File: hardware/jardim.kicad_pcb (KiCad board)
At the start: 2 copper layers, 100 x 100 mm, 81 parts, among them J1 DC_INPUT, J10 DHT22_AMB, J11 LIGHT_SENSOR_1, J12 LIGHT_SENSOR_2, J13 LEVEL_SENSOR_1, J14 LEVEL_SENSOR_2, J15 SOIL_HUMIDITY_SENSOR_1, J16 SOIL_HUMIDITY_SENSOR_2, J2 PUMP_1, J3 PUMP_2, J4 LIGHT_1, J5 LIGHT_2, J6 HEAT_1, J7 HEAT_2, J8 DS12B20_2, J9 DS18B20_1, Q1 FQP30N06L, Q2 FQP30N06L, Q3 FQP30N06L, Q4 FQP30N06L, Q5 FQP30N06L, Q6 FQP30N06L, Q7 BC337, SW1 SW_Push, SW2 SW_Push, SW3 SW_Push, SW4 SW_SPST, U1 AM2302, U2 DM-OLED096-636

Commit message: corrigido todos os modulos perifericos
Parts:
- removed C3, C6: 100uF 25V, Capacitor_THT:CP_Radial_D6.3mm_P2.50mm
- removed C4, C5: 100nF 50V, Capacitor_THT:C_Disc_D5.0mm_W2.5mm_P5.00mm
- H1: renamed from h1; value MountingHole_3.2mm_M3_Pad_Via -> MountingHole_Pad
- H2: renamed from h2; value MountingHole_3.2mm_M3_Pad_Via -> MountingHole_Pad
- H3: renamed from h3; value MountingHole_3.2mm_M3_Pad_Via -> MountingHole_Pad
- H4: renamed from h4; value MountingHole_3.2mm_M3_Pad_Via -> MountingHole_Pad
- J5: value LIGHT_2 -> LIGHG_2
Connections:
- net Net-(D1-A) renamed /PUMP_1_SW_NEG
- net Net-(D3-A) renamed /PUMP_2_SW_NEG
- net Net-(D6-K) renamed /LIGHT_1_SW_NEG
- net Net-(D7-K) renamed /LIGHT_2_SW_NEG
- net Net-(D8-K) renamed /HEATER_1_SW_NEG
- net Net-(D9-K) renamed /HEATER_2_SW_NEG
- H1 pad 1: (no net) -> GND
- H2 pad 1: (no net) -> GND
- H3 pad 1: (no net) -> GND
- H4 pad 1: (no net) -> GND
- R3 pad 1: +12V -> Net-(D2-A)
- R3 pad 2: Net-(D2-A) -> +12V
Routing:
- net +12V: track 286.4 -> 0.00 mm, vias 1 -> 0
- net +5V: track 241.2 -> 0.00 mm, vias 1 -> 0
- net +24V: track 194.4 -> 0.00 mm, vias 1 -> 0
- net /IO37: track 124.4 -> 0.00 mm
- net /IO11: track 98.3 -> 0.00 mm
- net /PUMP_2_SW_NEG: track 93.0 -> 0.00 mm
- net /IO9: track 76.6 -> 0.00 mm, vias 1 -> 0
- net /IO18: track 73.2 -> 0.00 mm
- net /IO12: track 66.2 -> 0.00 mm, vias 1 -> 0
- net /IO8: track 64.7 -> 0.00 mm, vias 1 -> 0
- net /IO36: track 59.2 -> 0.00 mm, vias 1 -> 0
- net /IO35: track 58.7 -> 0.00 mm
- net /IO10: track 58.6 -> 0.00 mm
- net /IO1: track 58.1 -> 0.00 mm, vias 1 -> 0
- net /IO17: track 55.8 -> 0.00 mm
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- removed copper zone on B.Cu, net GND
- removed copper zone on F.Cu, net GND

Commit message: lemure e usb c
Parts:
- added J18: USB_C_Receptacle_PowerOnly_6P, Connector_USB:USB_C_Receptacle_GCT_USB4125-xx-x_6P_TopMnt_Horizontal, F.Cu at (188.6, 118.7)
- added R22: 5.1k, Resistor_THT:R_Axial_DIN0207_L6.3mm_D2.5mm_P10.16mm_Horizontal, B.Cu at (163.0, 90.4)
- added R23: 5.1k, Resistor_THT:R_Axial_DIN0207_L6.3mm_D2.5mm_P10.16mm_Horizontal, B.Cu at (163.0, 94.5)
- moved H4 13.7 mm to (187.7, 132.1)
- moved SW1 8.25 mm to (175.2, 114.6)
- moved SW2 8.25 mm to (175.2, 122.2)
- moved SW3 8.25 mm to (175.2, 129.8)
- moved C2 2.59 mm to (170.8, 65.4)
- moved C1 1.27 mm to (164.5, 66.6)
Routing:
- net GND: track 0.00 -> 594.7 mm, vias 0 -> 1
- net +5V: track 0.00 -> 240.6 mm
- net +12V: track 0.00 -> 235.8 mm, vias 0 -> 2
- net +24V: track 0.00 -> 199.8 mm, vias 0 -> 1
- net /IO11: track 0.00 -> 107.0 mm
- net /PUMP_2_SW_NEG: track 0.00 -> 101.6 mm, vias 0 -> 1
- net /IO9: track 0.00 -> 89.7 mm, vias 0 -> 1
- net /IO18: track 0.00 -> 77.3 mm
- net /IO8: track 0.00 -> 70.0 mm, vias 0 -> 1
- net Net-(J18-CC1): track 0.00 -> 69.6 mm
- net /IO36: track 0.00 -> 63.0 mm, vias 0 -> 1
- net /IO35: track 0.00 -> 60.8 mm
- net /IO10: track 0.00 -> 58.4 mm
- net /IO13: track 0.00 -> 57.3 mm
- net /IO17: track 0.00 -> 56.1 mm
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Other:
- board text added: "Projetado no Brasil"
- board text removed: "DOWN"
- board text removed: "UP"

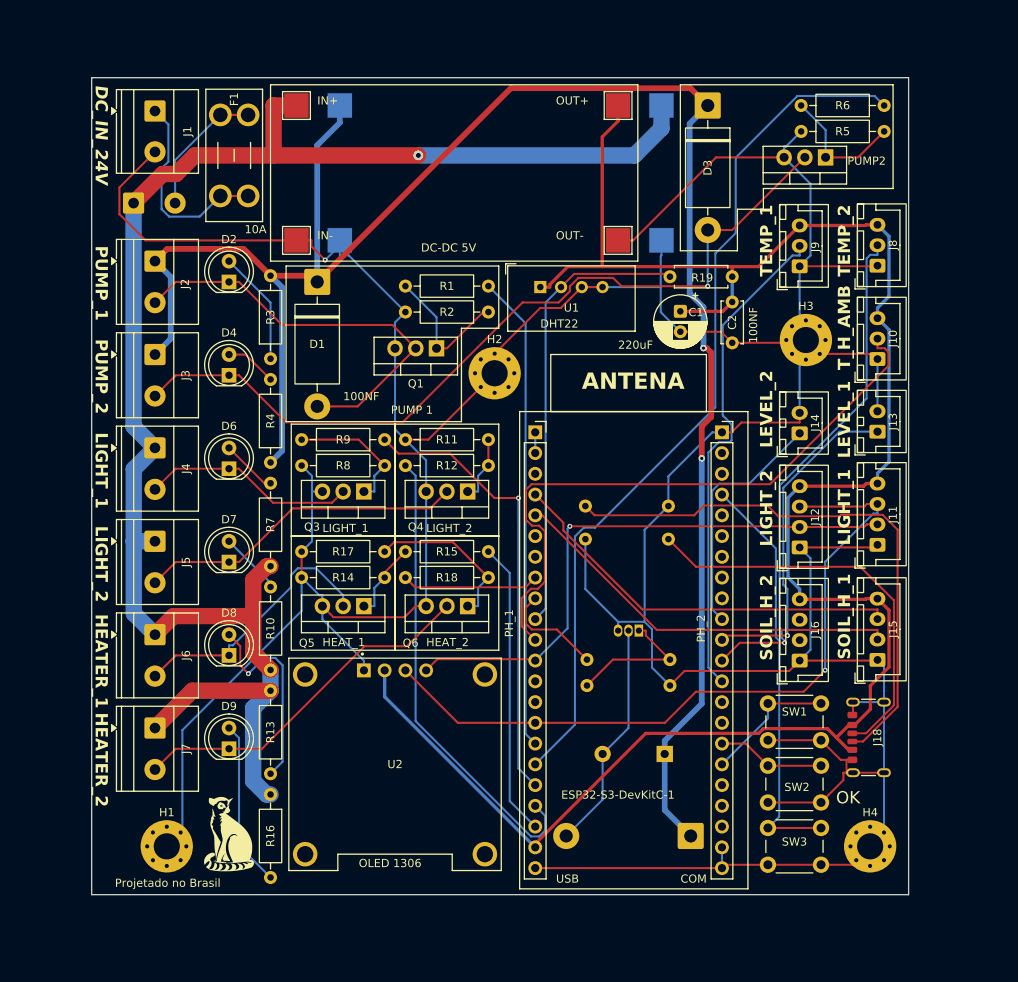
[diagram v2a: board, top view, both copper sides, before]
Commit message: pull up sensores, debaunce botoes
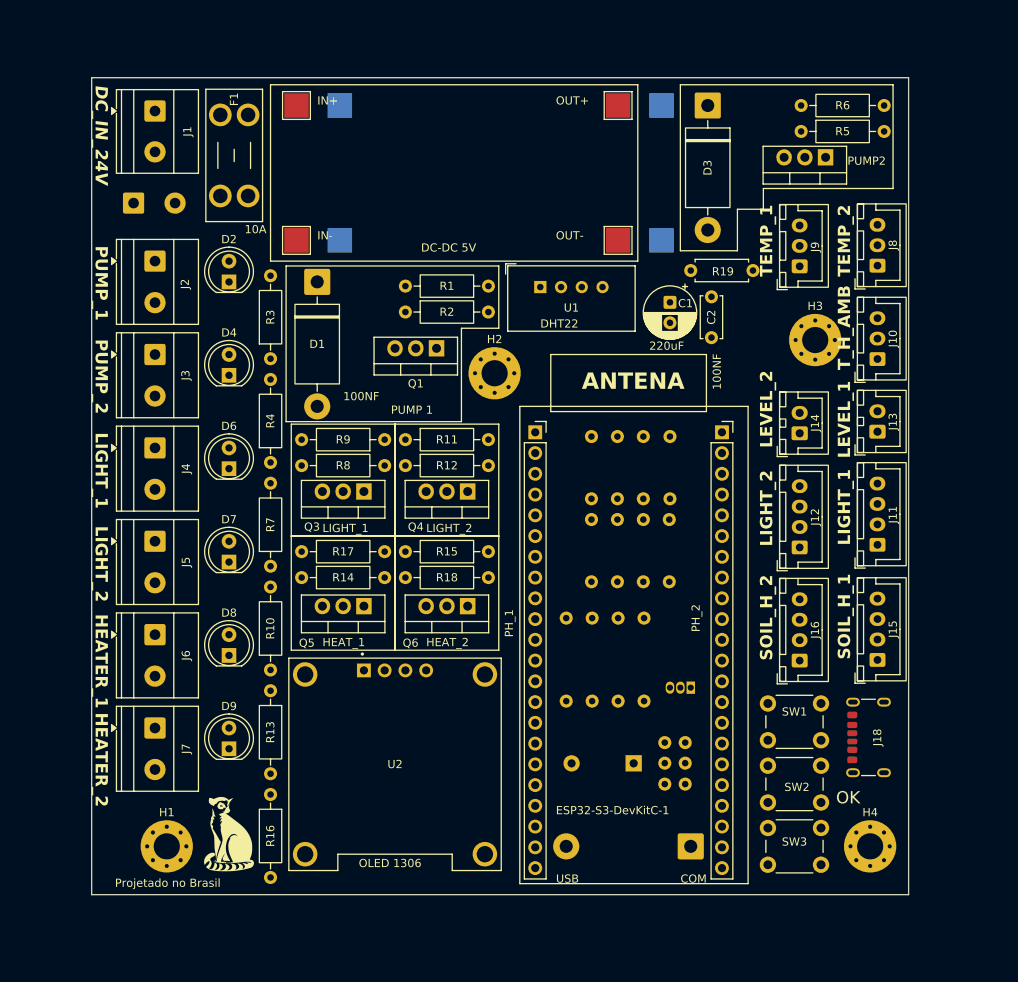
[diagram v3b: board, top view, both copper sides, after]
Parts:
- added C3: 100nf, Capacitor_THT:C_Disc_D3.0mm_W1.6mm_P2.50mm, B.Cu at (165.1, 119.4)
- added C4: 100nf, Capacitor_THT:C_Disc_D3.0mm_W1.6mm_P2.50mm, B.Cu at (165.1, 121.9)
- added C5: 100nf, Capacitor_THT:C_Disc_D3.0mm_W1.6mm_P2.50mm, B.Cu at (165.1, 124.5)
- added R27: 4.7k, Resistor_THT:R_Axial_DIN0207_L6.3mm_D2.5mm_P7.62mm_Horizontal, B.Cu at (163.2, 89.5)
- added R28: 4.7k, Resistor_THT:R_Axial_DIN0207_L6.3mm_D2.5mm_P7.62mm_Horizontal, B.Cu at (159.9, 89.5)
- added R29: 4.7k, Resistor_THT:R_Axial_DIN0207_L6.3mm_D2.5mm_P7.62mm_Horizontal, B.Cu at (156.8, 89.5)
- added R30: 4.7k, Resistor_THT:R_Axial_DIN0207_L6.3mm_D2.5mm_P7.62mm_Horizontal, B.Cu at (153.6, 89.5)
- added R31: 1k, Resistor_THT:R_Axial_DIN0207_L6.3mm_D2.5mm_P7.62mm_Horizontal, B.Cu at (153.6, 92.1)
- added R32: 1k, Resistor_THT:R_Axial_DIN0207_L6.3mm_D2.5mm_P7.62mm_Horizontal, B.Cu at (156.8, 92.1)
- added R33: 1k, Resistor_THT:R_Axial_DIN0207_L6.3mm_D2.5mm_P7.62mm_Horizontal, B.Cu at (159.9, 92.1)
- added R34: 1k, Resistor_THT:R_Axial_DIN0207_L6.3mm_D2.5mm_P7.62mm_Horizontal, B.Cu at (163.1, 92.1)
- F1: value 15A -> 10A
- moved R23 20.0 mm to (160.0, 114.3), turned to 90 degrees
- moved R22 15.0 mm to (156.8, 104.1), turned to -90 degrees
- moved R20 13.7 mm to (150.5, 104.1), turned to -90 degrees
- moved R21 12.6 mm to (153.7, 104.1), turned to -90 degrees
- moved Q7 9.44 mm to (165.7, 112.7)
- moved BZ1 3.97 mm to (158.8, 121.9)
- moved R19 2.65 mm to (173.4, 61.6)
- moved C2 2.62 mm to (168.3, 64.8)
- moved C1 1.68 mm to (163.2, 65.5)
- moved D5 1.27 mm to (165.7, 132.1)
- moved H3 1.14 mm to (181.0, 70.1)
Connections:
- net Net-(J1-Pin_1) renamed /VIN_RAW
- J15 pad 2: /IO5 -> unconnected-(J15-Pin_2-Pad2)
- J15 pad 3: /IO4 -> /IO5
- J16 pad 3: unconnected-(J16-Pin_3-Pad3) -> /IO4
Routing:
- net GND: track 594.7 -> 0.00 mm, vias 1 -> 0
- net +5V: track 240.6 -> 0.00 mm
- net +12V: track 235.8 -> 0.00 mm, vias 2 -> 0
- net +24V: track 199.8 -> 0.00 mm, vias 1 -> 0
- net /IO11: track 107.0 -> 0.00 mm
- net /PUMP_2_SW_NEG: track 101.6 -> 0.00 mm, vias 1 -> 0
- net /IO9: track 89.7 -> 0.00 mm, vias 1 -> 0
- net /IO18: track 77.3 -> 0.00 mm
- net /IO8: track 70.0 -> 0.00 mm, vias 1 -> 0
- net Net-(J18-CC1): track 69.6 -> 0.00 mm
- net /IO36: track 63.0 -> 0.00 mm, vias 1 -> 0
- net /IO35: track 60.8 -> 0.00 mm
- net /IO10: track 58.4 -> 0.00 mm
- net /IO13: track 57.3 -> 0.00 mm
- net /IO17: track 56.1 -> 0.00 mm
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
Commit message: ajustes
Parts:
- removed R2: 10k, Resistor_THT:R_Axial_DIN0207_L6.3mm_D2.5mm_P10.16mm_Horizontal
- moved U2 1.35 mm to (129.5, 123.4)
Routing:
- added copper zone on B.Cu, net GND
- added copper zone on F.Cu, net GND
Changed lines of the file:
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@@
 	(footprint "oled:MODULE_DM-OLED096-636"
 		(layer "F.Cu")
-		(at 129.54 122.04)
+		(at 129.54 123.395)
 		(property "Reference" "U2"
 			(at 0 0 0)
@@
 	(footprint "Capacitor_THT:CP_Radial_D6.3mm_P2.50mm"
 		(layer "F.Cu")
-		(at 163.195 65.492621 -90)
+		(at 163.195 65.4926 -90)
 		(descr "CP, Radial series, Radial, pin pitch=2.50mm, diameter=6.3mm, height=7mm, Electrolytic Capacitor")
 		(tags "CP Radial series Radial pin pitch 2.50mm diameter 6.3mm height 7mm Electrolytic Capacitor")
@@
 		)
 	)
-	(footprint "Resistor_THT:R_Axial_DIN0207_L6.3mm_D2.5mm_P10.16mm_Horizontal"
-		(layer "F.Cu")
-		(at 130.81 66.675)
-		(descr "Resistor, Axial_DIN0207 series, Axial, Horizontal, pin pitch=10.16mm, 0.25W = 1/4W, length*diameter=6.3*2.5mm^2, http://cdn-reichelt.de/documents/datenblatt/B400/1_4W%23YAG.pdf")
-		(tags "Resistor Axial_DIN0207 series Axial Horizontal pin pitch 10.16mm 0.25W = 1/4W length 6.3mm diameter 2.5mm")
-		(property "Reference" "R2"
-			(at 5.08 0 0)
-			(layer "F.SilkS")
-			(effects
-				(font
-					(size 1 1)
-					(thickness 0.15)
-				)
-			)
-		)
-		(property "Value" "10k"
-			(at 5.08 2.37 0)
-			(layer "F.Fab")
-			(effects
-				(font
-					(size 1 1)
-					(thickness 0.15)
-				)
-			)
-		)
-		(property "Datasheet" ""
-			(at 0 0 0)
-			(layer "F.Fab")
-			(hide yes)
-			(effects
-				(font
-					(size 1.27 1.27)
-				)
-			)
-		)
-		(property "Description" "Resistor"
-			(at 0 0 0)
-			(layer "F.Fab")
-			(hide yes)
-			(effects
-				(font
-					(size 1.27 1.27)
-				)
-			)
-		)
-		(property ki_fp_filters "R_*")
-		(sheetname "/")
-		(sheetfile "jardim.kicad_sch")
-		(units
-			(unit
-				(name "A")
-				(pins "1" "2")
-			)
-		)
-		(attr through_hole)
-		(duplicate_pad_numbers_are_jumpers no)
-		(fp_line
-			(start 1.04 0)
-			(end 1.81 0)
-			(stroke
-				(width 0.12)
-				(type solid)
-			)
-			(layer "F.SilkS")
-		)
-		(fp_line
-			(start 9.12 0)
-			(end 8.35 0)
-			(stroke
-				(width 0.12)
-				(type solid)
-			)
-			(layer "F.SilkS")
-		)
-		(fp_rect
-			(start 1.81 -1.37)
-			(end 8.35 1.37)
-			(stroke
-				(width 0.12)
-				(type solid)
-			)
-			(fill no)
-			(layer "F.SilkS")
-		)
-		(fp_rect
-			(start -1.05 -1.5)
-			(end 11.21 1.5)
-			(stroke
-				(width 0.05)
-				(type solid)
-			)
-			(fill no)
-			(layer "F.CrtYd")
-		)
-		(fp_line
-			(start 0 0)
-			(end 1.93 0)
-			(stroke
-				(width 0.1)
-				(type solid)
-			)
-			(layer "F.Fab")
-		)
-		(fp_line
-			(start 10.16 0)
-			(end 8.23 0)
-			(stroke
-				(width 0.1)
-				(type solid)
-			)
-			(layer "F.Fab")
-		)
-		(fp_rect
-			(start 1.93 -1.25)
-			(end 8.23 1.25)
-			(stroke
-				(width 0.1)
-				(type solid)
-			)
-			(fill no)
-			(layer "F.Fab")
-		)
-		(fp_text user "${REFERENCE}"
-			(at 5.08 0 0)
-			(layer "F.Fab")
-			(effects
-				(font
-					(size 1 1)
-					(thickness 0.15)
-				)
-			)
-		)
-		(pad "1" thru_hole circle
-			(at 0 0)
-			(size 1.6 1.6)
-			(drill 0.8)
-			(layers "*.Cu" "*.Mask")
-			(remove_unused_layers no)
-			(net "GND")
-			(pintype "passive")
-		)
-		(pad "2" thru_hole circle
-			(at 10.16 0)
-			(size 1.6 1.6)
-			(drill 0.8)
-			(layers "*.Cu" "*.Mask")
-			(remove_unused_layers no)
-			(net "Net-(Q1-G)")
-			(pintype "passive")
-		)
-		(embedded_fonts no)
-		(model "kicad-embed://R_Axial_DIN0207_L6.3mm_D2.5mm_P10.16mm_Horizontal.step"
-			(offset
-				(xyz 0 0 0)
-			)
-			(scale
-				(xyz 1 1 1)
-			)
-			(rotate
-				(xyz 0 0 0)
-			)
-		)
-	)
 	(footprint "Button_Switch_THT:SW_PUSH_6mm"
 		(layer "F.Cu")
@@
 		(sheetname "/")
 		(sheetfile "jardim.kicad_sch")
+		(units
+			(unit
+				(name "A")
+				(pins "1" "2")
+			)
+		)
 		(attr through_hole)
 		(duplicate_pad_numbers_are_jumpers no)
@@
 		(sheetname "/")
 		(sheetfile "jardim.kicad_sch")
+		(units
+			(unit
+				(name "A")
+				(pins "1" "2")
+			)
+		)
 		(attr through_hole)
 		(duplicate_pad_numbers_are_jumpers no)
@@
 		(sheetname "/")
 		(sheetfile "jardim.kicad_sch")
+		(units
+			(unit
+				(name "A")
+				(pins "1" "2")
+			)
+		)
 		(attr through_hole)
 		(duplicate_pad_numbers_are_jumpers no)
@@
 	)
 	(gr_text "OLED 1306"
-		(at 125.095 134.74 0)
+		(at 125.095 136.095 0)
 		(layer "F.SilkS")
 		(effects
@@
 			)
 		)
+	)
+	(zone
+		(net "GND")
+		(layers "F.Cu" "B.Cu")
+		(hatch edge 0.5)
+		(connect_pads
+			(clearance 0.5)
+		)
+		(min_thickness 0.25)
+		(fill yes
+			(thermal_gap 0.5)
+			(thermal_bridge_width 0.5)
+			(island_removal_mode 0)
+		)
+		(polygon
+			(pts
+				(xy 83.185 31.115) (xy 83.185 146.05) (xy 203.835 146.685) (xy 202.565 30.48)
+			)
+		)

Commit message: sem avisos, pronto para rotear
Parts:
- added R2: 10k, Resistor_THT:R_Axial_DIN0207_L6.3mm_D2.5mm_P10.16mm_Horizontal, F.Cu at (124.5, 67.3)
- moved R19 19.1 mm to (154.3, 62.9), turned to 0 degrees
- moved R5 6.71 mm to (172.5, 44.3)
- moved R6 6.71 mm to (182.7, 41.2)
- moved U1 6.37 mm to (141.0, 64.1)
- moved R1 6.35 mm to (134.6, 63.5)
- moved C2 4.93 mm to (172.1, 61.7)
- moved C1 4.61 mm to (167.0, 62.9)
- moved Q1 3.18 mm to (131.4, 71.1)
- moved Q2 2.72 mm to (179.5, 47.6)
- moved J2 1.91 mm to (98.3, 60.4)
- moved J3 1.91 mm to (98.3, 71.9)
- moved J4 1.91 mm to (98.3, 83.3)
- moved J5 1.91 mm to (98.3, 94.7)
- moved J6 1.91 mm to (98.3, 106.2)
- moved J7 1.91 mm to (98.3, 117.6)
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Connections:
- net Net-(SW4-B) renamed /VIN_AFTER_FUSE
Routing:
- net +24V: track 0.00 -> 257.2 mm
- net +12V: track 0.00 -> 244.2 mm, vias 0 -> 1
- net +5V: track 0.00 -> 243.7 mm
- net /IO11: track 0.00 -> 102.0 mm, vias 0 -> 1
- net /PUMP_2_SW_NEG: track 0.00 -> 94.7 mm
- net /IO9: track 0.00 -> 77.9 mm
- net /IO36: track 0.00 -> 72.7 mm, vias 0 -> 1
- net /IO10: track 0.00 -> 70.0 mm, vias 0 -> 1
- net /IO17: track 0.00 -> 68.5 mm, vias 0 -> 2
- net /IO37: track 0.00 -> 68.3 mm, vias 0 -> 1
- net /IO18: track 0.00 -> 67.9 mm
- net /IO1: track 0.00 -> 67.4 mm
- net /IO35: track 0.00 -> 65.0 mm
- net /IO8: track 0.00 -> 63.7 mm
- net /IO38: track 0.00 -> 54.3 mm
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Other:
- board text removed: "10k"

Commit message: netlist completa
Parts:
- moved H3 0.50 mm to (179.7, 70.5)
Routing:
- net +24V: track 257.2 -> 157.5 mm, vias 0 -> 1
- net +5V: track 243.7 -> 203.4 mm, vias 0 -> 1
- net /IO36: track 72.7 -> 32.9 mm
- net +12V: track 244.2 -> 263.2 mm, vias 1 -> 0
- net /IO18: track 67.9 -> 78.7 mm, vias 0 -> 1
- net Net-(D8-A): track 19.1 -> 29.9 mm
- net /IO12: track 53.8 -> 63.9 mm, vias 1 -> 0
- net /IO16: track 23.4 -> 14.2 mm
- net /IO10: track 70.0 -> 61.1 mm, vias 1 -> 0
- net /IO11: track 102.0 -> 110.6 mm, vias 1 -> 0
- net /IO38: track 54.3 -> 61.7 mm
- net /IO17: track 68.5 -> 61.4 mm, vias 2 -> 0
- net Net-(J18-CC1): track 31.7 -> 38.6 mm
- net /IO9: track 77.9 -> 84.2 mm, vias 0 -> 1
- net /IO35: track 65.0 -> 71.1 mm, vias 0 -> 1
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
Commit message: 0 erros. 100%
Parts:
- moved R6 10.2 mm to (172.5, 40.9), turned to 0 degrees
- moved C3 1.73 mm to (165.6, 117.1)
- moved H3 1.45 mm to (178.8, 69.3)
- moved C1 1.41 mm to (166.6, 64.3)
- moved C5 1.26 mm to (165.6, 125.0)
- moved C4 0.62 mm to (165.6, 120.9)
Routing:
- net +5V: track 203.4 -> 271.1 mm
- net +24V: track 157.5 -> 212.0 mm
- net /IO36: track 32.9 -> 85.1 mm, vias 1 -> 0
- net +12V: track 263.2 -> 240.5 mm
- net /IO11: track 110.6 -> 125.5 mm
- net /IO18: track 78.7 -> 64.0 mm
- net /IO12: track 63.9 -> 51.0 mm, vias 0 -> 1
- net /IO38: track 61.7 -> 70.2 mm
- net /IO1: track 65.2 -> 73.5 mm
- net Net-(D8-A): track 29.9 -> 21.8 mm
- net Net-(Q2-G): track 16.8 -> 8.81 mm
- net /IO47: track 24.6 -> 31.2 mm
- net Net-(J18-CC1): track 38.6 -> 32.3 mm
- net Net-(BZ1--): track 27.6 -> 33.1 mm
- net GND: track 0.00 -> 4.17 mm
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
